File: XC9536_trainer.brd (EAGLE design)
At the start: 100 x 80 mm, 7 parts, among them IC1 XC9536_44VQ, U1 FTS31XS-U

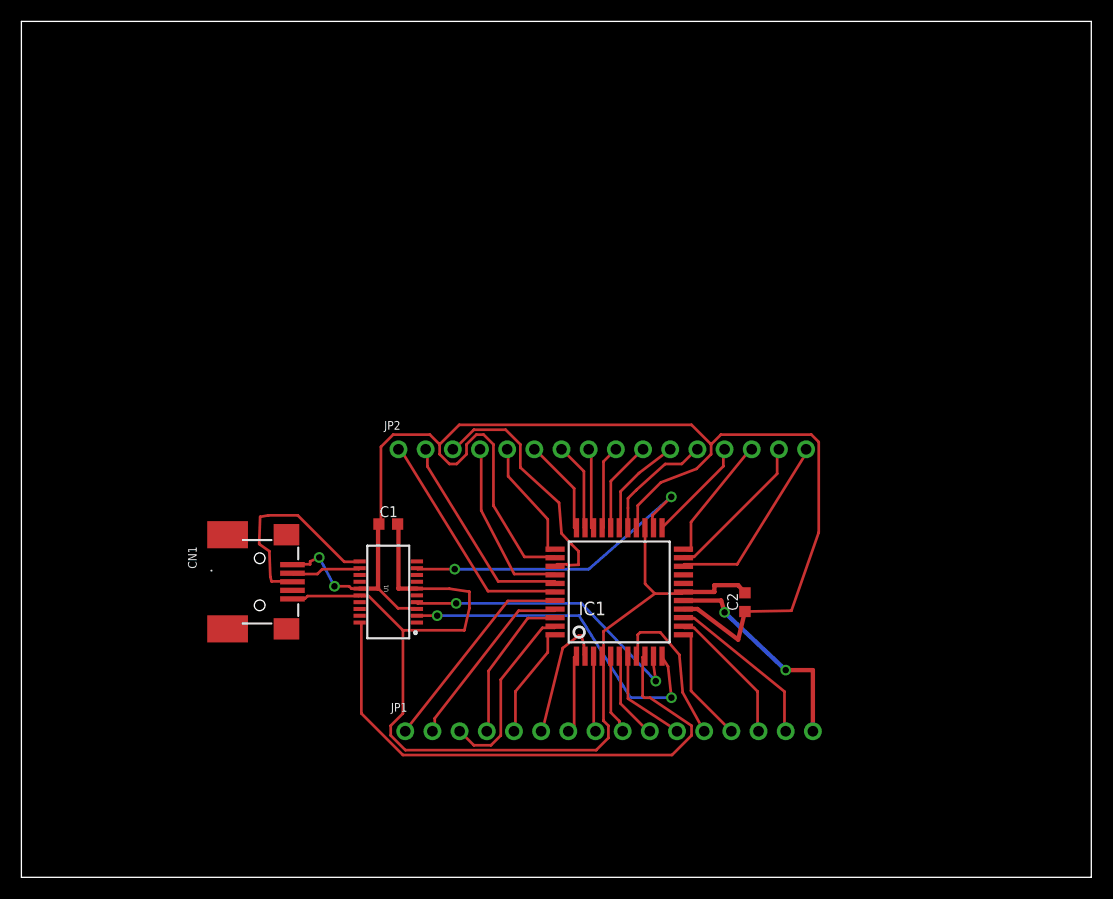
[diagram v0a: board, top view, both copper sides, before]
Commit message: Changed board size to fit into 5x5cm, added some silkscreen and possibly made it possible to use it in a breadboard.
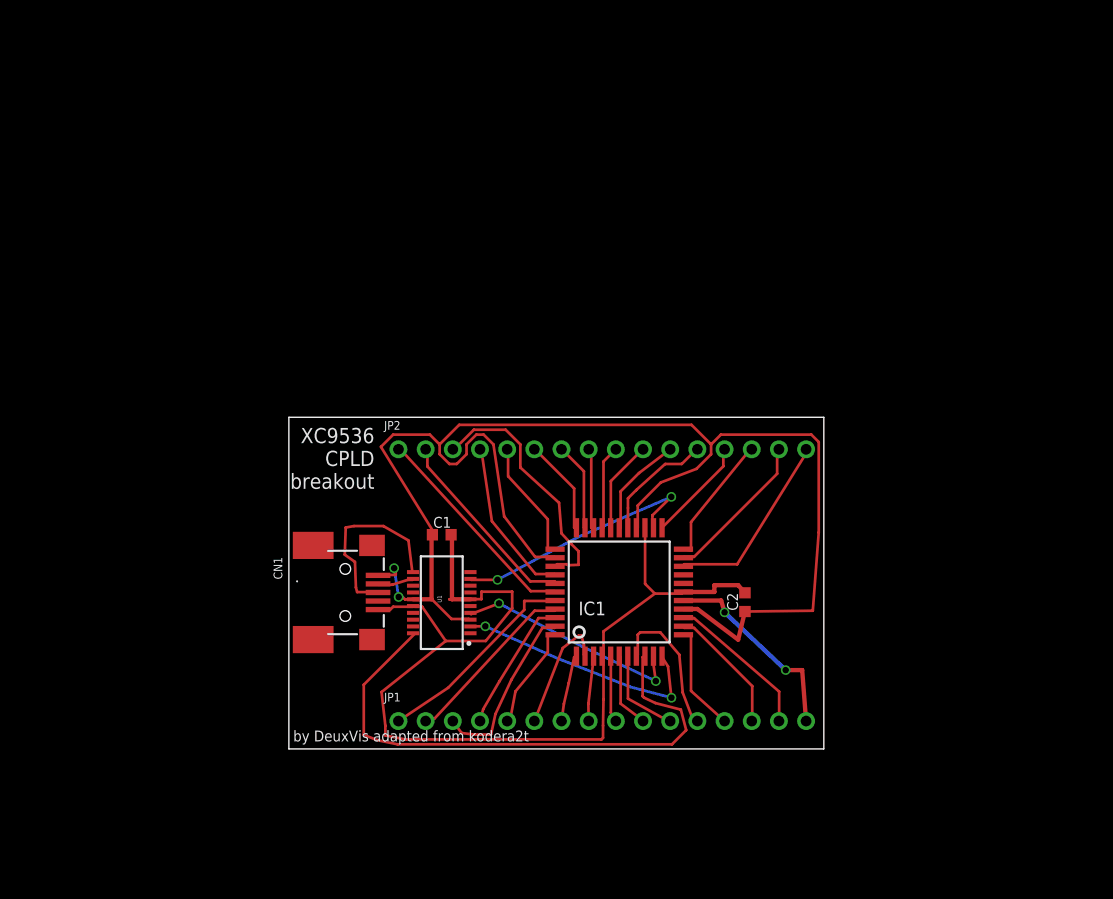
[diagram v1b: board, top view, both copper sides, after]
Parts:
- C1, C2: value (none) -> 0.1µF
- moved CN1 8.06 mm to (29.3, 26.6)
- moved C1 5.10 mm to (39.3, 32.0)
- moved U1 5.10 mm to (39.3, 25.7)
- moved JP1 1.14 mm to (54.3, 14.6)
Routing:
- net N$6: track 32.1 -> 24.1 mm
- net N$5: track 27.9 -> 21.7 mm
- net N$7: track 30.1 -> 24.3 mm
- net N$2: track 6.56 -> 3.44 mm
- net B_ZERO15: track 20.8 -> 18.9 mm
- net B_ZERO3: track 14.5 -> 12.7 mm
- net N$1: track 19.6 -> 17.8 mm
- net B_ONE0: track 22.1 -> 20.5 mm
- net VCC: track 135.5 -> 136.9 mm
- net B_ZERO14: track 15.7 -> 14.3 mm
- net B_ONE3: track 16.4 -> 15.2 mm
- net B_ZERO13: track 13.3 -> 12.1 mm
- net B_ONE1: track 19.8 -> 18.7 mm
- net B_ZERO9: track 8.28 -> 7.16 mm
- net B_ZERO12: track 11.2 -> 10.1 mm
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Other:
- board size 100 x 80 mm -> 50 x 31 mm
- board text added: "XC9536 CPLD breakout"
- board text added: "by DeuxVis adapted from kodera2t"

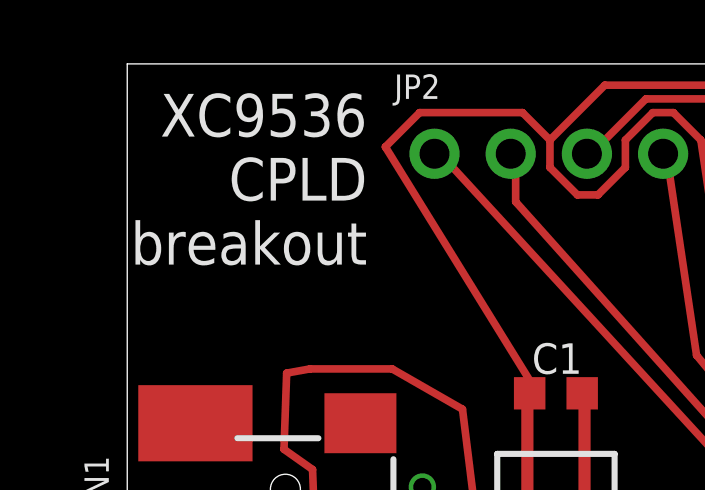
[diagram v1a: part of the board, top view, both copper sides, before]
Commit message: Corrected some silkscreen, adding gerber. Ready for first test production batch.
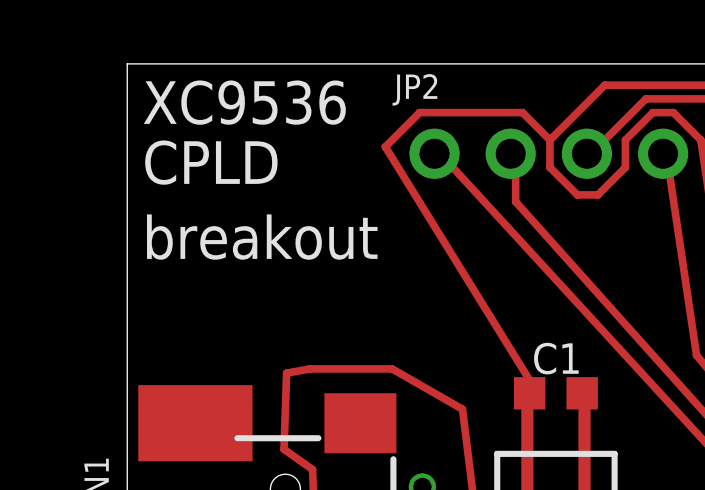
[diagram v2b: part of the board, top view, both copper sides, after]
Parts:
- IC1: value XC9536_44VQ -> XC9536
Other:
- board text added: "CPLD"
- board text added: "XC9536"
- board text added: "breakout"
- board text removed: "XC9536 CPLD breakout"
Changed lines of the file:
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@@
 <setting verticaltext="up"/>
 </settings>
-<grid distance="1" unitdist="mm" unit="mm" style="lines" multiple="1" display="yes" altdistance="0.5" altunitdist="mm" altunit="mm"/>
+<grid distance="0.5" unitdist="mm" unit="mm" style="lines" multiple="1" display="yes" altdistance="0.1" altunitdist="mm" altunit="mm"/>
 <layers>
 <layer number="1" name="Top" color="4" fill="1" visible="yes" active="yes"/>
@@
 <rectangle x1="37.385" y1="21.225" x2="41.195" y2="30.115" layer="43"/>
 <rectangle x1="50.8" y1="21.59" x2="60.96" y2="31.75" layer="43"/>
-<text x="33" y="42" size="1.4224" layer="112" rot="R180">XC9536
-CPLD
-breakout</text>
+<text x="25.5" y="41" size="1.4224" layer="112" rot="R180" align="top-right">XC9536</text>
 <text x="25.4" y="12.7" size="1.016" layer="121">by DeuxVis adapted from kodera2t</text>
+<text x="25.5" y="39" size="1.4224" layer="112" rot="R180" align="top-right">CPLD</text>
+<text x="25.5" y="36.5" size="1.4224" layer="112" rot="R180" align="top-right">breakout</text>
 </plain>
 <attributes>
@@
 <elements>
 <element name="CN1" library="OLED_mod" package="USB-MINIB_LARGER" value="" x="29.2725" y="26.6225" rot="R270"/>
-<element name="IC1" library="xilinx-xc9" package="SQFP-S-10X10-44" value="XC9536_44VQ" x="55.88" y="26.67">
+<element name="IC1" library="xilinx-xc9" package="SQFP-S-10X10-44" value="XC9536" x="55.88" y="26.67">
 <attribute name="OC_NEWARK" value="98K3377" x="55.88" y="26.67" size="1.778" layer="27" display="off"/>
 <attribute name="MPN" value="XC9536-15VQG44C" x="55.88" y="26.67" size="1.778" layer="27" display="off"/>
@@
 </board>
 </drawing>
-<compatibility>
-<note version="6.3" minversion="6.2.2" severity="warning">
-Since Version 6.2.2 text objects can contain more than one line,
-which will not be processed correctly with this version.
-</note>
-</compatibility>
 </eagle>
